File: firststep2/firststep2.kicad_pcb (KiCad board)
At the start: 2 copper layers, 43.2 x 17.8 mm, 6 parts, among them J1 Analog, J2 Digital

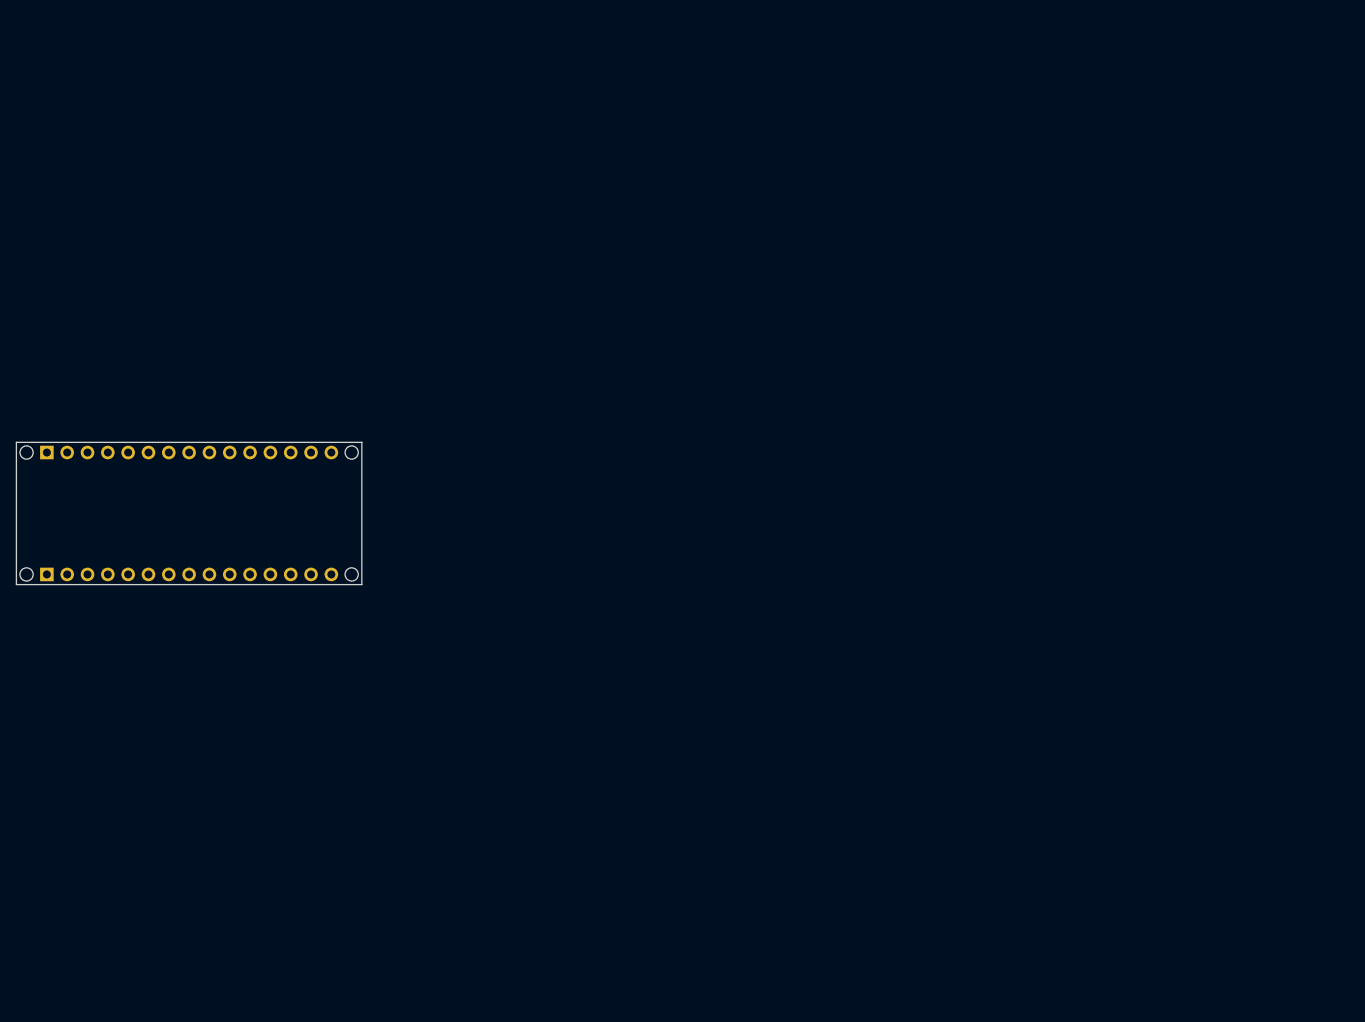
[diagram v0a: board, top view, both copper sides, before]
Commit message: added atmega_logic, changed lm to tl
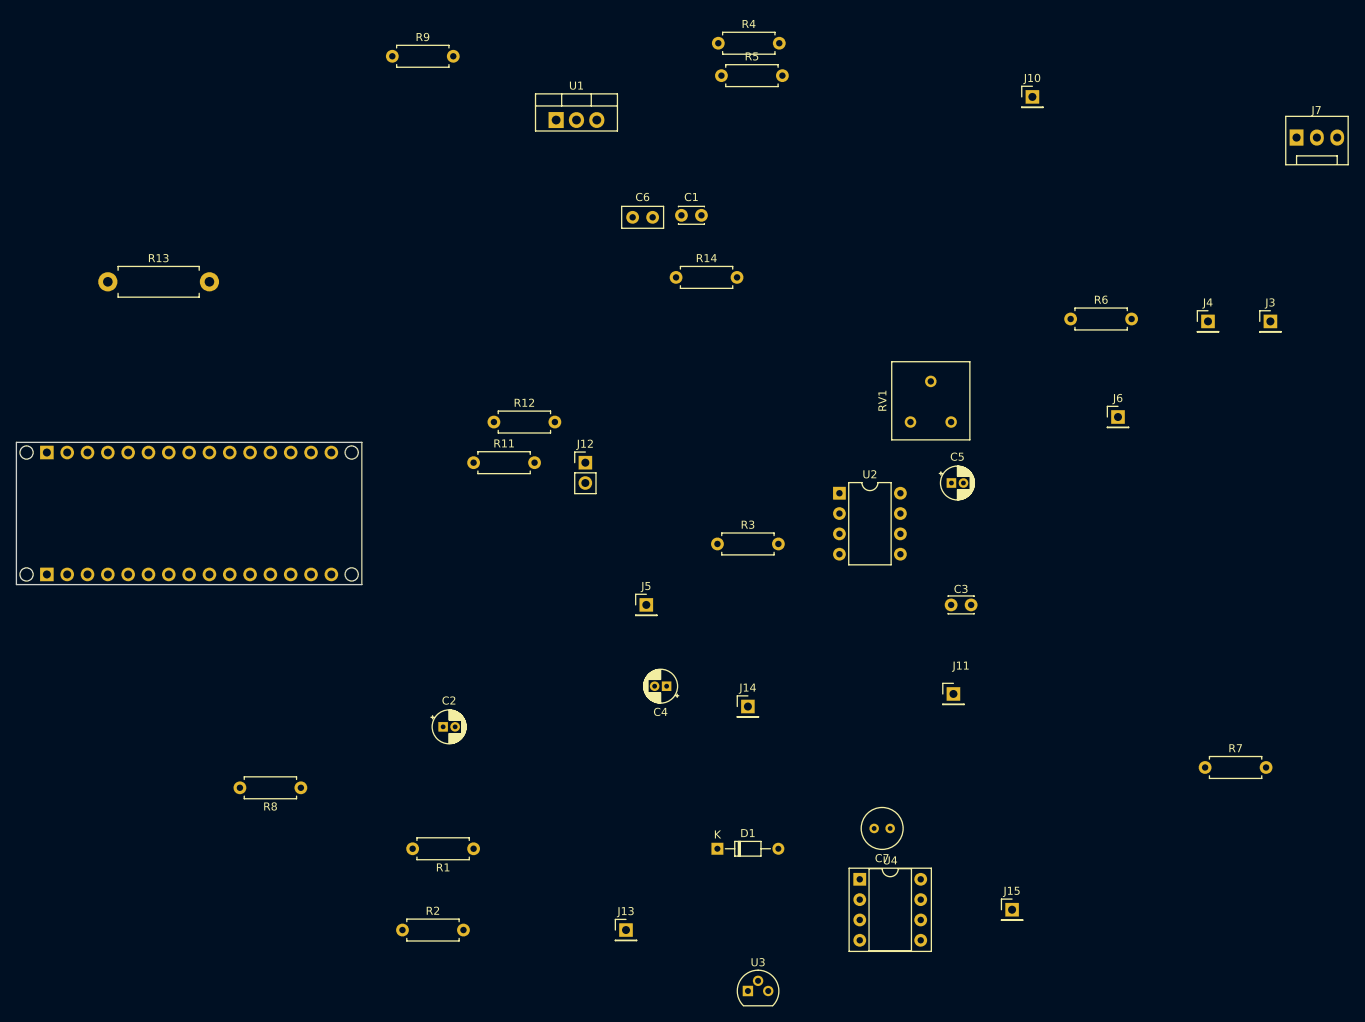
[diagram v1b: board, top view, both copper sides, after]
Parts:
- added C1: 10n, Capacitor_THT:C_Disc_D3.0mm_W2.0mm_P2.50mm, F.Cu at (183.1, 53.8)
- added C2: 3,3u, Capacitor_THT:CP_Radial_D4.0mm_P1.50mm, F.Cu at (153.3, 117.8)
- added C3: 100n, Capacitor_THT:C_Disc_D3.0mm_W2.0mm_P2.50mm, F.Cu at (216.8, 102.5)
- added C4: 1u, Capacitor_THT:CP_Radial_D4.0mm_P1.50mm, F.Cu at (181.3, 112.7)
- added C5: 1u, Capacitor_THT:CP_Radial_D4.0mm_P1.50mm, F.Cu at (216.9, 87.3)
- added C6: 100n, Capacitor_THT:C_Disc_D5.0mm_W2.5mm_P2.50mm, F.Cu at (177.0, 54.1)
- added C7: 10u, Capacitor_THT:C_Radial_D5.0mm_H5.0mm_P2.00mm, F.Cu at (209.2, 130.5)
- added D1: D_Zener, Diode_THT:D_DO-34_SOD68_P7.62mm_Horizontal, F.Cu at (187.6, 133.0)
- added J10: Arduino_A7, Connector_PinHeader_2.54mm:PinHeader_1x01_P2.54mm_Vertical, F.Cu at (227.0, 39.0)
- added J11: Arduino_D6, Connector_PinHeader_2.54mm:PinHeader_1x01_P2.54mm_Vertical, F.Cu at (217.1, 113.7)
- added J12: RELAY_SW, Connector_PinHeader_2.54mm:PinHeader_1x02_P2.54mm_Vertical, F.Cu at (171.1, 84.8)
- added J13: RELAY_PWR, Connector_PinHeader_2.54mm:PinHeader_1x01_P2.54mm_Vertical, F.Cu at (176.2, 143.2)
- added J14: Arduino_D9, Connector_PinHeader_2.54mm:PinHeader_1x01_P2.54mm_Vertical, F.Cu at (191.4, 115.2)
- added J15: Conn_FET, Connector_PinHeader_2.54mm:PinHeader_1x01_P2.54mm_Vertical, F.Cu at (224.5, 140.6)
- added J2: Conn_01x03_Male, Connector:FanPinHeader_1x03_P2.54mm_Vertical, F.Cu at (260.0, 44.1)
- added J3: POWER12, Connector_PinHeader_2.54mm:PinHeader_1x01_P2.54mm_Vertical, F.Cu at (256.8, 67.1)
- added J4: Conn_5V, Connector_PinHeader_2.54mm:PinHeader_1x01_P2.54mm_Vertical, F.Cu at (248.9, 67.1)
- added J5: Conn_GND, Connector_PinHeader_2.54mm:PinHeader_1x01_P2.54mm_Vertical, F.Cu at (178.7, 102.5)
- added J6: Arduino_A6, Connector_PinHeader_2.54mm:PinHeader_1x01_P2.54mm_Vertical, F.Cu at (237.7, 79.0)
- added R11: 22K, Resistor_THT:R_Axial_DIN0207_L6.3mm_D2.5mm_P7.62mm_Horizontal, F.Cu at (157.2, 84.8)
- added R12: 22K, Resistor_THT:R_Axial_DIN0207_L6.3mm_D2.5mm_P7.62mm_Horizontal, F.Cu at (159.7, 79.7)
- added R13: 10, Resistor_THT:R_Axial_DIN0411_L9.9mm_D3.6mm_P12.70mm_Horizontal, F.Cu at (111.4, 62.1)
- added R14: 10K, Resistor_THT:R_Axial_DIN0207_L6.3mm_D2.5mm_P7.62mm_Horizontal, F.Cu at (182.5, 61.6)
- added R2: 330, Resistor_THT:R_Axial_DIN0207_L6.3mm_D2.5mm_P7.62mm_Horizontal, F.Cu at (157.2, 133.0)
- added R2: 330, Resistor_THT:R_Axial_DIN0207_L6.3mm_D2.5mm_P7.62mm_Horizontal, F.Cu at (148.3, 143.2)
- added R3: 330, Resistor_THT:R_Axial_DIN0207_L6.3mm_D2.5mm_P7.62mm_Horizontal, F.Cu at (187.6, 94.9)
- added R4: 470, Resistor_THT:R_Axial_DIN0207_L6.3mm_D2.5mm_P7.62mm_Horizontal, F.Cu at (187.7, 32.3)
- added R5: 220, Resistor_THT:R_Axial_DIN0207_L6.3mm_D2.5mm_P7.62mm_Horizontal, F.Cu at (188.1, 36.4)
- added R6: 270, Resistor_THT:R_Axial_DIN0207_L6.3mm_D2.5mm_P7.62mm_Horizontal, F.Cu at (231.8, 66.8)
- added R7: 330, Resistor_THT:R_Axial_DIN0207_L6.3mm_D2.5mm_P7.62mm_Horizontal, F.Cu at (248.6, 122.9)
- added R8: 150K, Resistor_THT:R_Axial_DIN0207_L6.3mm_D2.5mm_P7.62mm_Horizontal, F.Cu at (135.6, 125.4)
- added R9: 10K, Resistor_THT:R_Axial_DIN0207_L6.3mm_D2.5mm_P7.62mm_Horizontal, F.Cu at (147.0, 34.0)
- added RV1: R_Potentiometer, Potentiometer_THT:Potentiometer_Bourns_3386F_Vertical, F.Cu at (216.8, 79.7)
- added U1: LM317_TO-220, Package_TO_SOT_THT:TO-220-3_Vertical, F.Cu at (167.5, 41.9)
- added U2: TL431LP, Package_TO_SOT_THT:TO-92, F.Cu at (191.4, 150.8)
- added U2: TL072, Package_DIP:DIP-8_W7.62mm, F.Cu at (202.9, 88.6)
- added U4: MIC4428, Package_DIP:DIP-8_W7.62mm_Socket, F.Cu at (205.4, 136.8)
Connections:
- net +3V3 renamed +3.3V
